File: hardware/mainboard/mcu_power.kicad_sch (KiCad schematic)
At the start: 85 parts, among them Q201 MMBT3904, Q202 IRLML2244, SW201 Tactile switch, SW202 Tactile switch, SW203 Tactile switch, SW204 Tactile switch, SW205 Tactile switch, SW206 Tactile switch, SW207 Tactile switch, SW208 Tactile switch, U201 STM32F405RGTx, U202 TPS7A2033, U203 TP6841S6, Y201 8 MHz

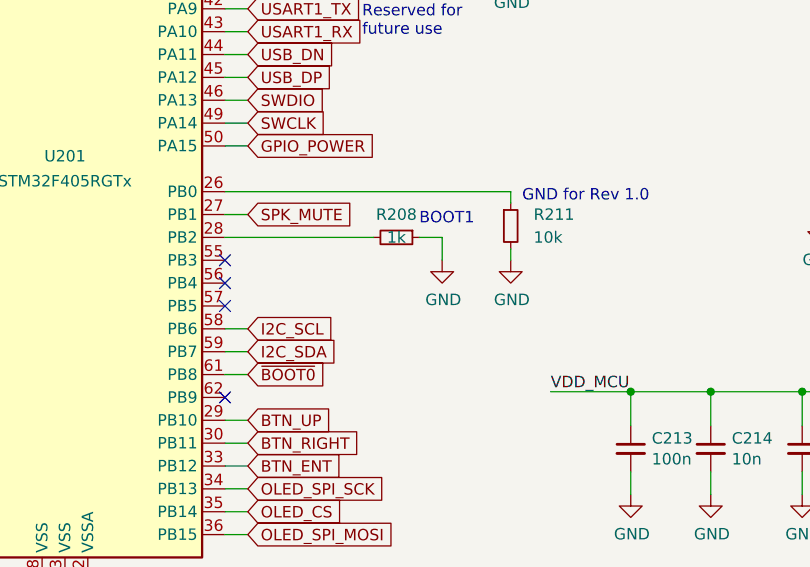
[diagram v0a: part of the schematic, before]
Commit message: Updated mainboard
Fixed dimension issues: moved some connectors closer to the edge of the board. Made the board 3.3mm longer.
Added pull-ups to the I2C bus.
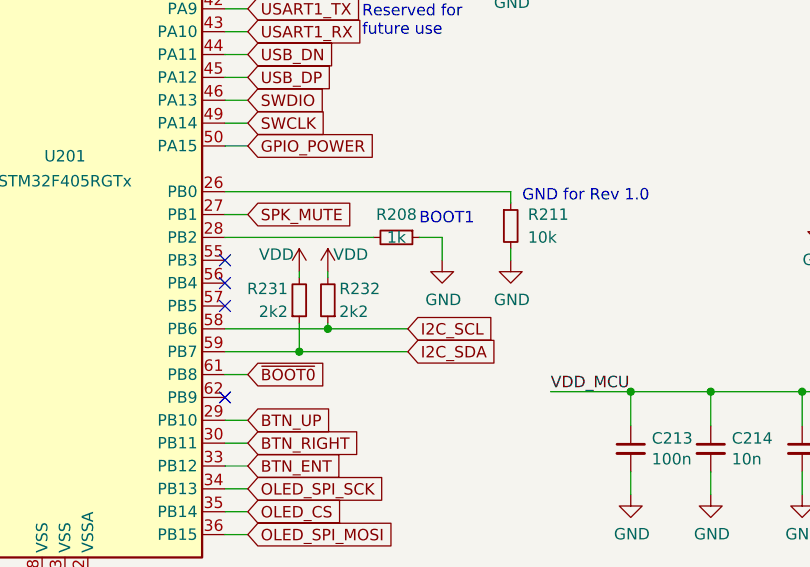
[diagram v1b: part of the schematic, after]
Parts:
- added R231, R232: 2k2, Resistor_SMD:R_0603_1608Metric, symbol Device:R_Small
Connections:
- net I2C_SCL: now also R232.1
- net I2C_SDA: now also R231.1
- net VDD: now also R231.2, R232.2

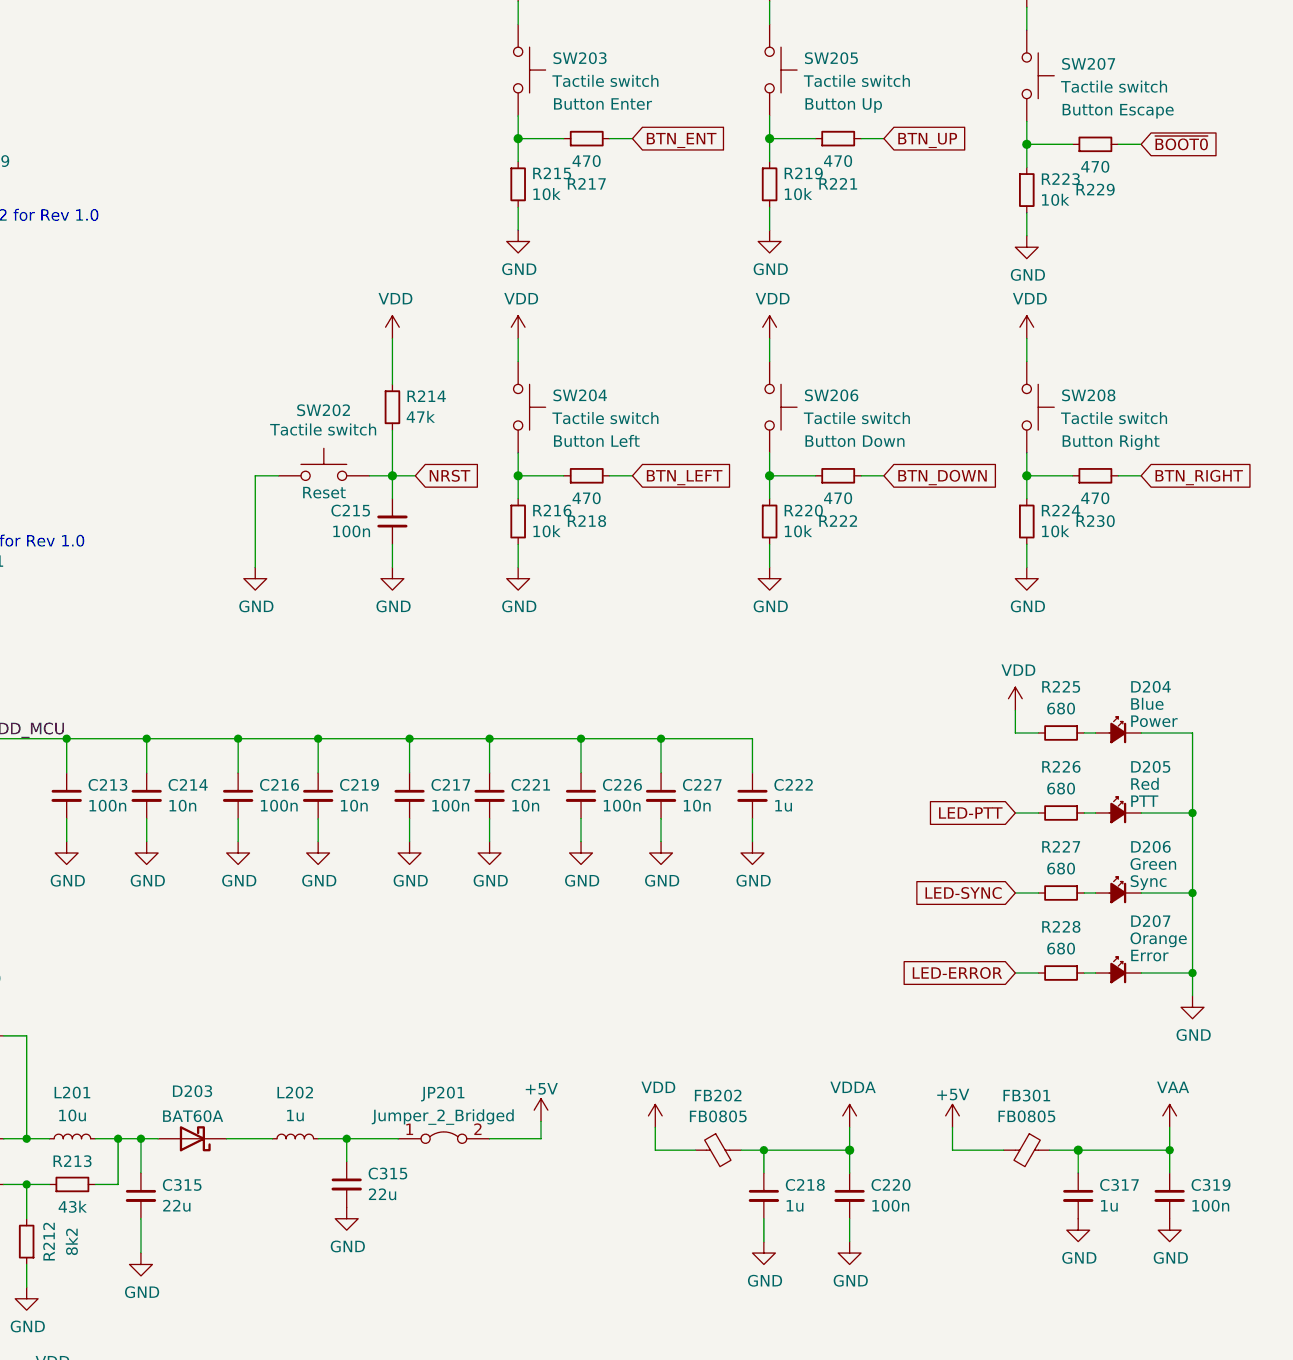
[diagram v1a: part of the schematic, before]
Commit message: Updated mainboard
Replaced OHIS speaker resistors with larger 100 ohms resistors
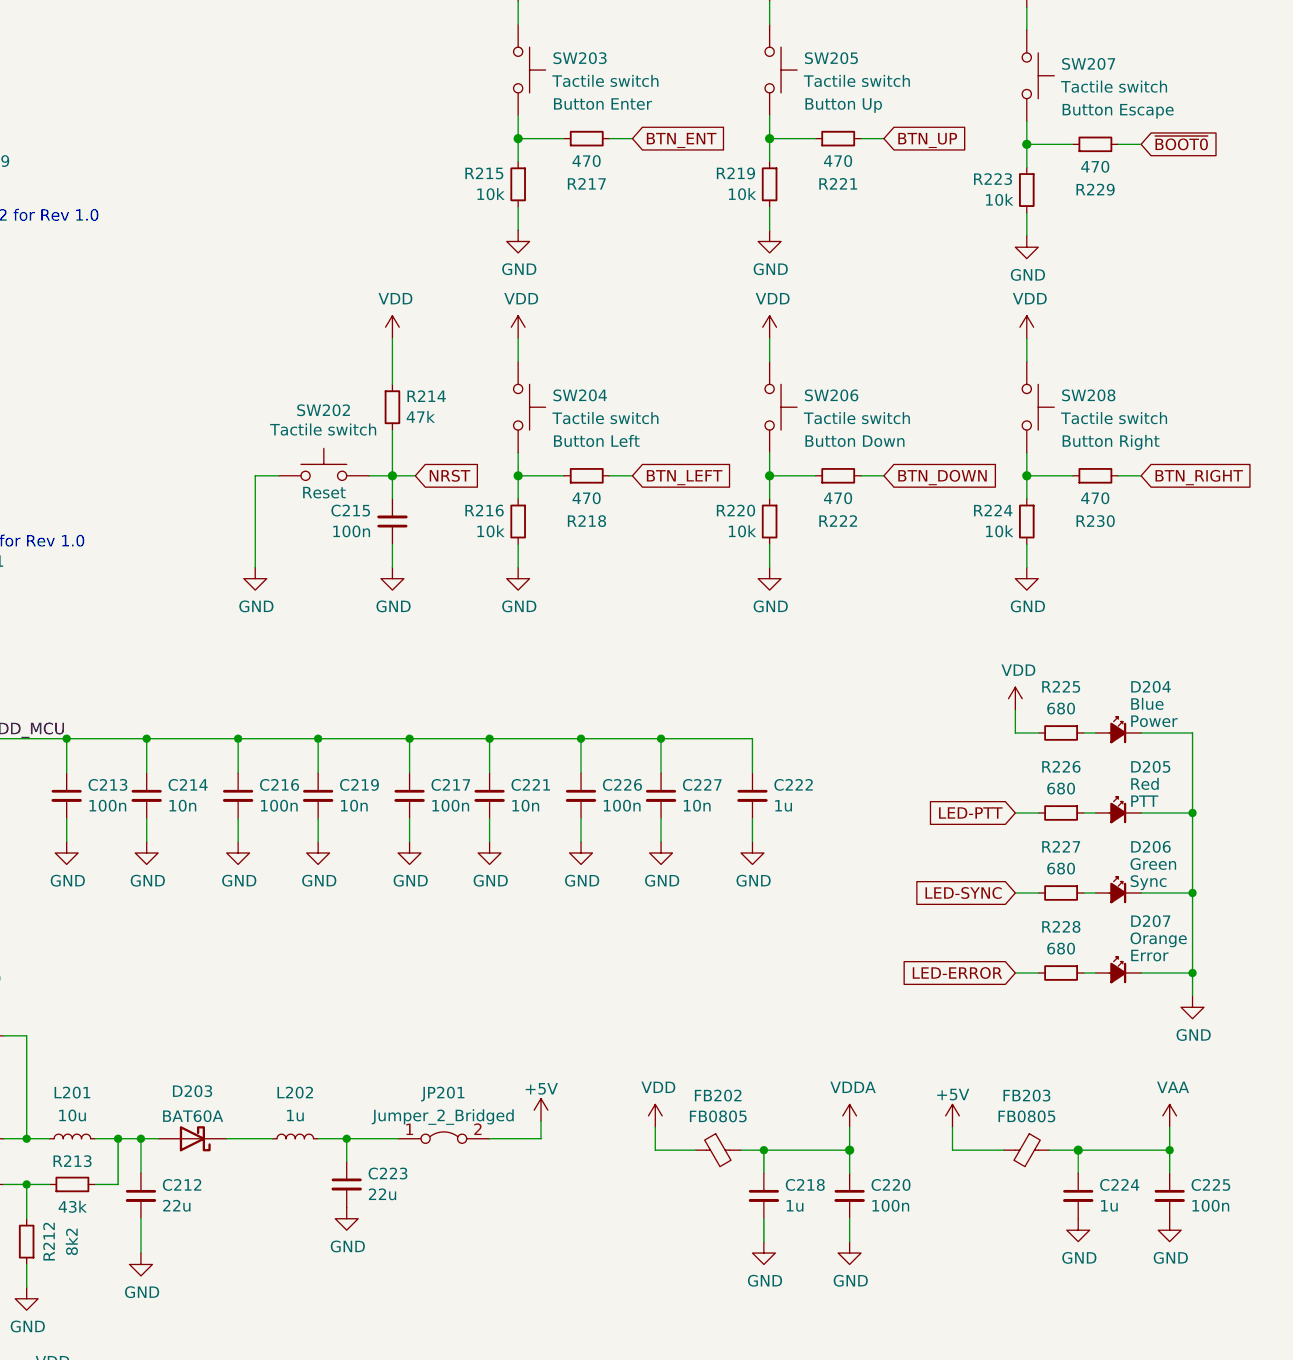
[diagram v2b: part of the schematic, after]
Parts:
- renumbered C315 to C212, C315 to C223, C317 to C224, C319 to C225, FB301 to FB203
